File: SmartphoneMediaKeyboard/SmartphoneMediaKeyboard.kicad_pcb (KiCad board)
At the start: 2 copper layers, 74.5 x 56 mm, 19 parts, among them J4 Conn_02x05_Top_Bottom, SW1 SW_NEXT, SW2 SW_PAUSE, U1 ATtiny2313-20S, Y1 12MHz

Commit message: Wiring done, too big to my taste but will have to do.
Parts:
- moved R1 2.59 mm to (172.5, 105.5)
- moved R5 2.00 mm to (178.5, 106.2)
- moved C4 1.50 mm to (180.0, 116.5)
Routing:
- net /D-: track 0.00 -> 72.9 mm, vias 0 -> 2
- net Net-(U1-PB1): track 6.50 -> 68.2 mm, vias 0 -> 2
- net GND: track 190.3 -> 236.3 mm, vias 0 -> 4
- net /D+: track 0.00 -> 44.2 mm, vias 0 -> 2
- net +5V: track 33.1 -> 65.0 mm, vias 0 -> 2
- net Net-(D4-A): track 0.00 -> 27.8 mm
- net Net-(D1-A): track 0.00 -> 25.3 mm, vias 0 -> 2
- net Net-(U1-PB0): track 17.2 -> 23.7 mm
- net Net-(D1-K): track 9.78 -> 7.78 mm
- net Net-(D4-K): track 15.5 -> 14.6 mm
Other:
- board size 74.5 x 56 mm -> 74 x 49.5 mm

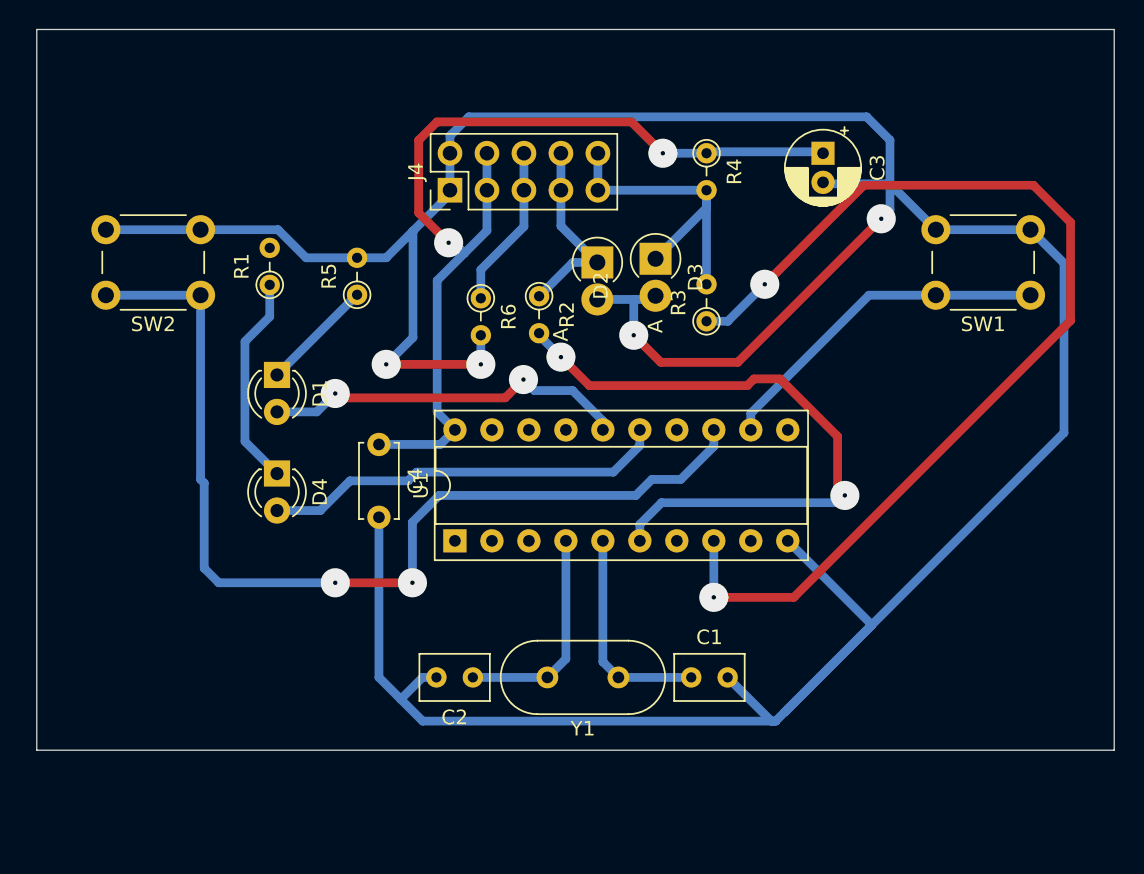
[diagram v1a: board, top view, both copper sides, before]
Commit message: Produced the board at home, and added some comments on the circuit for future me readability
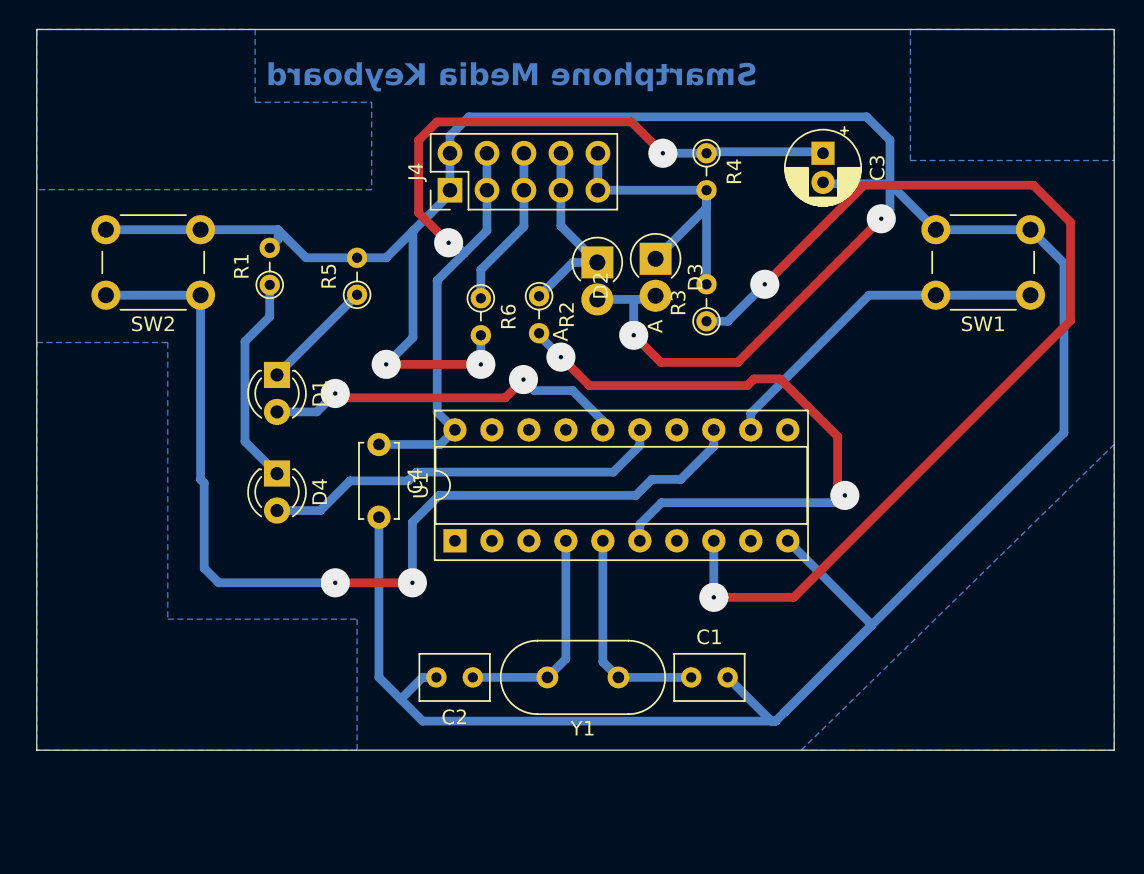
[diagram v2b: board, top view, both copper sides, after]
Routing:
- net GND: track 236.3 -> 237.8 mm
- added copper zone on B.Cu, net GND
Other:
- board text added: "Smartphone Media Keyboard"
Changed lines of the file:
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@@
 		(allow_soldermask_bridges_in_footprints no)
 		(pcbplotparams
-			(layerselection 0x00010fc_ffffffff)
-			(plot_on_all_layers_selection 0x0000000_00000000)
+			(layerselection 0x0000000_fffffffe)
+			(plot_on_all_layers_selection 0x0001000_00000000)
 			(disableapertmacros no)
 			(usegerberextensions no)
@@
 			(outputformat 1)
 			(mirror no)
-			(drillshape 1)
+			(drillshape 0)
 			(scaleselection 1)
 			(outputdirectory "")
@@
 		(layer "Edge.Cuts")
 	)
+	(gr_text "Smartphone Media Keyboard"
+		(at 206 92 0)
+		(layer "B.Cu")
+		(effects
+			(font
+				(size 1.5 1.5)
+				(thickness 0.3)
+				(bold yes)
+			)
+			(justify left bottom mirror)
+		)
+	)
 	(segment
 		(start 187 111)
@@
 	)
 	(segment
+		(start 172.5 103)
+		(end 173.07 102.43)
+		(width 0.6)
+		(layer "B.Cu")
+		(net 1)
+	)
+	(segment
 		(start 161.25 101.75)
 		(end 167.75 101.75)
@@
 	)
 	(segment
+		(start 173.07 102.43)
+		(end 173.07 101.75)
+		(width 0.6)
+		(layer "B.Cu")
+		(net 1)
+	)
+	(segment
 		(start 206.95 135.5)
 		(end 207.25 135.5)
@@
 		(net 24)
 	)
+	(zone
+		(net 1)
+		(net_name "GND")
+		(layer "B.Cu")
+		(hatch edge 0.5)
+		(priority 2)
+		(connect_pads
+			(clearance 0.5)
+		)
+		(min_thickness 0.25)
+		(filled_areas_thickness no)
+		(fill yes
+			(thermal_gap 0.5)
+			(thermal_bridge_width 0.5)
+		)
+		(polygon
+			(pts
+				(xy 209 137.5) (xy 230.5 116.5) (xy 230.5 137.5)
+			)
+		)
+	)
+	(zone
+		(net 1)
+		(net_name "GND")
+		(layer "B.Cu")
+		(hatch edge 0.5)
+		(priority 3)
+		(connect_pads
+			(clearance 0.5)
+		)
+		(min_thickness 0.25)
+		(filled_areas_thickness no)
+		(fill yes
+			(thermal_gap 0.5)
+			(thermal_bridge_width 0.5)
+		)
+		(polygon
+			(pts
+				(xy 216.5 88) (xy 216.5 97) (xy 230.5 97) (xy 230.5 88)
+			)
+		)
+	)
+	(zone
+		(net 1)
+		(net_name "GND")
+		(layer "B.Cu")
+		(hatch edge 0.5)
+		(connect_pads
+			(clearance 0.5)
+		)
+		(min_thickness 0.25)
+		(filled_areas_thickness no)
+		(fill yes
+			(thermal_gap 0.5)
+			(thermal_bridge_width 0.5)
+		)
+		(polygon
+			(pts
+				(xy 156.5 88) (xy 171.5 88) (xy 171.5 93) (xy 179.5 93) (xy 179.5 99) (xy 156.5 99)
+			)
+		)
+	)
+	(zone
+		(net 1)
+		(net_name "GND")
+		(layer "B.Cu")
+		(hatch edge 0.5)
+		(priority 1)
+		(connect_pads
+			(clearance 0.5)
+		)
+		(min_thickness 0.25)
+		(filled_areas_thickness no)
+		(fill yes
+			(thermal_gap 0.5)
+			(thermal_bridge_width 0.5)
+		)
+		(polygon
+			(pts
+				(xy 156.5 109.5) (xy 165.5 109.5) (xy 165.5 128.5) (xy 178.5 128.5) (xy 178.5 137.5) (xy 156.5 137.5)
+			)
+		)
+	)
 )
